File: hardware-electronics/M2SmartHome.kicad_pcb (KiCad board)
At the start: 4 copper layers, 22 x 76 mm, 207 parts, among them J1 M.2-Key-M-edge-connector, J2 Micro_SD_Card_Det_Hirose_DM3AT, J3 CONMHF1-SMD-T, J4 CONMHF1-SMD-T, U1 RTL8188FTV-VC-CG, U10 24AA04T-I_OT, U2 EMMC16G-MW28-01E10, U3 PI7C9X440SLBFDE, U4 24AA04T-I_OT, U5 CP2102N-A02-GQFN20, U6 24AA04T-I_OT, U7 EFR32MG21B020F1024IM32-B, U8 USB2244-AEZG-06, U9 USB2244-AEZG-06, Y1 ABM8-12.000MHZ-B2-T, Y2 ECS-240-10-47-CKM-TR, Y3 ECS-240-10-47-CKM-TR, Y5 ABM8-40.000MHZ-B2-T

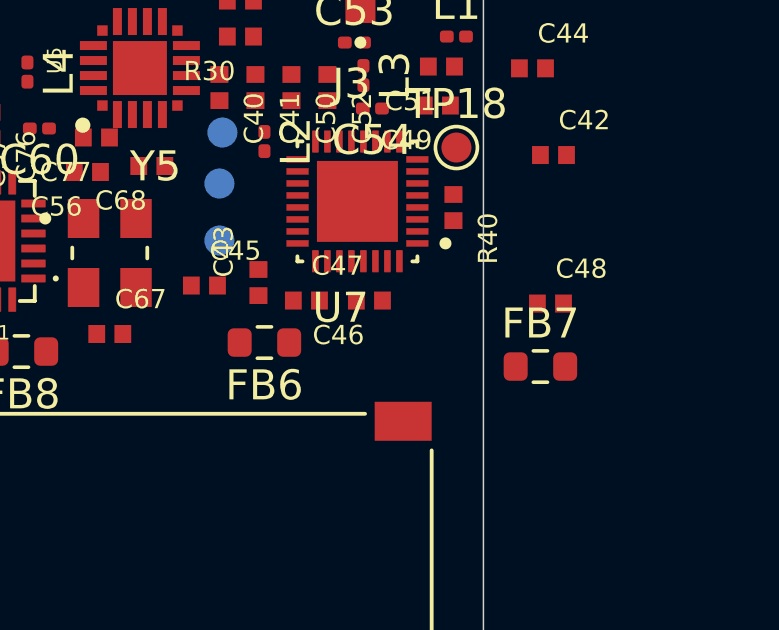
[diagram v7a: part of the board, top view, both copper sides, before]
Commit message: [#15] Defined net class for PCIe
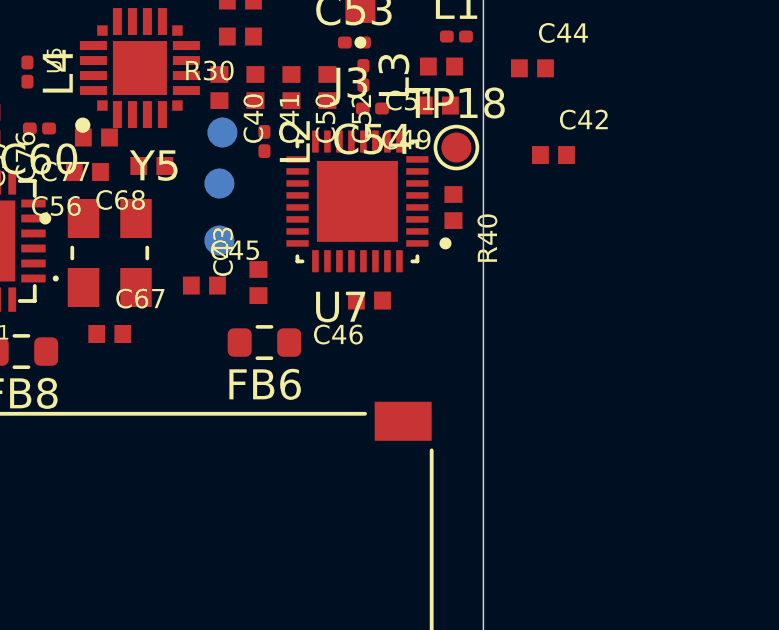
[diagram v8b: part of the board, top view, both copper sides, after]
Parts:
- removed C47: C_100n_0402, M2SmartHomeFootprints:C_0402
- removed C48: C_1uF_0402, M2SmartHomeFootprints:C_0402
- removed FB7: FB_120R_0603, M2SmartHomeFootprints:FB_0603
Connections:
- net /pcie-usb-bridge/PERN- renamed /PCIE.PERN-
- net /pcie-usb-bridge/PERP+ renamed /PCIE.PERP+
- net /pcie-usb-bridge/PETN- renamed /PCIE.PETN-
- net /pcie-usb-bridge/PETP+ renamed /PCIE.PETP+
- net /pcie-usb-bridge/REFCKLN- renamed /PCIE.REFCLKN-
- net /pcie-usb-bridge/REFCLKP+ renamed /PCIE.REFCLKP+
- C42 pad 1: Net-(U7-DECOUPLE) -> +3V3_Thread
- U7 pad 24: Net-(U7-DECOUPLE) -> +3V3_Thread
